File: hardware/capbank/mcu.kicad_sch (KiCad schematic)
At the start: 19 parts, among them J3 Conn_01x02, J4 Conn_01x02, J5 Conn_01x06, SW2 SW_SPST, U6 ATtiny84A-P, Y1 16MHz

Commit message: Small hardware changes
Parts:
- removed TP1: ~, TestPoint:TestPoint_THTPad_1.5x1.5mm_Drill0.7mm, symbol Connector:TestPoint
- removed U6: ATtiny84A-P, Package_DIP:DIP-14_W7.62mm, symbol MCU_Microchip_ATtiny:ATtiny84A-P
- added U8: ATtiny84A-SS, Package_SO:SOIC-14_3.9x8.7mm_P1.27mm, symbol MCU_Microchip_ATtiny:ATtiny84A-SS
- Y1: footprint (none) -> PCM_Crystal_Handsoldering_AKL:Resonator_SMD_muRata_CSTxExxV-3Pin_3.0x1.1mm_BigPads
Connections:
- net GND: now also U8.14 (GND)
- net HVSP_CLK_FSK_IN: now also U8.10 (PA3)
- net HVSP_SDI_RELAY1: now also U8.13 (AREF/PA0)
- net HVSP_SDO_RELAY3: now also U8.11 (PA2)
- net HVSP_SII_RELAY2: now also U8.12 (PA1)
- net PRG_MOSI_I2C_SDA: now also U8.7 (PA6)
- net PRG_SCK_I2C_SCL: now also U8.9 (PA4)
- net SCK: now also U8.5 (PB2)
- net SDI: now also U8.6 (PA7)
- net VDD: now also U8.1 (VCC)
- net XTAL1: now also U8.2 (XTAL1/PB0)
- net XTAL2: now also U8.3 (XTAL2/PB1)
- net ~{CS}: now also U8.8 (PA5)
- net ~{RESET}: now also U8.4 (~{RESET}/PB3)
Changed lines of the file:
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@@
-	)
-	(junction
-		(at 64.77 90.17)
-		(diameter 0)
-		(color 0 0 0 0)
 	)
 	(junction
@@
 	(wire
 		(pts
-			(xy 64.77 90.17) (xy 78.74 90.17)
-		)
-		(stroke
-			(width 0)
-			(type default)
-		)
-	)
-	(wire
-		(pts
 			(xy 195.58 38.1) (xy 195.58 36.83)
 		)
@@
 	(wire
 		(pts
-			(xy 59.69 90.17) (xy 64.77 90.17)
+			(xy 59.69 90.17) (xy 78.74 90.17)
 		)
 		(stroke
@@
 	)
 	(symbol
+		(lib_id "MCU_Microchip_ATtiny:ATtiny84A-SS")
+		(at 243.84 130.81 0)
+		(unit 1)
+		(exclude_from_sim no)
+		(in_bom yes)
+		(on_board yes)
+		(dnp no)
+		(fields_autoplaced yes)
+		(property "Reference" "U8"
+			(at 229.87 129.5399 0)
+			(effects
+				(font
+					(size 1.27 1.27)
+				)
+				(justify right)
+			)
+		)
+		(property "Value" "ATtiny84A-SS"
+			(at 229.87 132.0799 0)
+			(effects
+				(font
+					(size 1.27 1.27)
+				)
+				(justify right)
+			)
+		)
+		(property "Footprint" "Package_SO:SOIC-14_3.9x8.7mm_P1.27mm"
+			(at 243.84 130.81 0)
+			(effects
+				(font
+					(size 1.27 1.27)
+					(italic yes)
+				)
+				(hide yes)
+			)
+		)
+		(property "Datasheet" "http://ww1.microchip.com/downloads/en/DeviceDoc/doc8183.pdf"
+			(at 243.84 130.81 0)
+			(effects
+				(font
+					(size 1.27 1.27)
+				)
+				(hide yes)
+			)
+		)
+		(property "Description" "20MHz, 8kB Flash, 512B SRAM, 512B EEPROM, debugWIRE, SOIC-14"
+			(at 243.84 130.81 0)
+			(effects
+				(font
+					(size 1.27 1.27)
+				)
+				(hide yes)
+			)
+		)
+		(pin "4"
+		)
+		(pin "7"
+		)
+		(pin "2"
+		)
+		(pin "3"
+		)
+		(pin "5"
+		)
+		(pin "8"
+		)
+		(pin "6"
+		)
+		(pin "9"
+		)
+		(pin "10"
+		)
+		(pin "11"
+		)
+		(pin "12"
+		)
+		(pin "13"
+		)
+		(pin "14"
+		)
+		(pin "1"
+		)
+		(instances
+			(project ""
+				(path "/461cb8a1-2d60-44a8-88b5-d61a3ba14a84/d9c36704-5831-4033-b353-abc8255d1c86"
+					(reference "U8")
+					(unit 1)
+				)
+			)
+		)
+	)
+	(symbol
 		(lib_id "power:GND")
 		(at 93.98 97.79 0)
@@
 	)
 	(symbol
-		(lib_id "MCU_Microchip_ATtiny:ATtiny84A-P")
-		(at 243.84 130.81 0)
-		(unit 1)
-		(exclude_from_sim no)
-		(in_bom yes)
-		(on_board yes)
-		(dnp no)
-		(fields_autoplaced yes)
-		(property "Reference" "U6"
-			(at 229.87 129.5399 0)
-			(effects
-				(font
-					(size 1.27 1.27)
-				)
-				(justify right)
-			)
-		)
-		(property "Value" "ATtiny84A-P"
-			(at 229.87 132.0799 0)
-			(effects
-				(font
-					(size 1.27 1.27)
-				)
-				(justify right)
-			)
-		)
-		(property "Footprint" "Package_DIP:DIP-14_W7.62mm"
-			(at 243.84 130.81 0)
-			(effects
-				(font
-					(size 1.27 1.27)
-					(italic yes)
-				)
-				(hide yes)
-			)
-		)
-		(property "Datasheet" "http://ww1.microchip.com/downloads/en/DeviceDoc/doc8183.pdf"
-			(at 243.84 130.81 0)
-			(effects
-				(font
-					(size 1.27 1.27)
-				)
-				(hide yes)
-			)
-		)
-		(property "Description" "20MHz, 8kB Flash, 512B SRAM, 512B EEPROM, debugWIRE, DIP-14"
-			(at 243.84 130.81 0)
-			(effects
-				(font
-					(size 1.27 1.27)
-				)
-				(hide yes)
-			)
-		)
-		(pin "11"
-		)
-		(pin "5"
-		)
-		(pin "12"
-		)
-		(pin "13"
-		)
-		(pin "2"
-		)
-		(pin "8"
-		)
-		(pin "9"
-		)
-		(pin "14"
-		)
-		(pin "6"
-		)
-		(pin "7"
-		)
-		(pin "3"
-		)
-		(pin "4"
-		)
-		(pin "1"
-		)
-		(pin "10"
-		)
-		(instances
-			(project ""
-				(path "/461cb8a1-2d60-44a8-88b5-d61a3ba14a84/d9c36704-5831-4033-b353-abc8255d1c86"
-					(reference "U6")
-					(unit 1)
-				)
-			)
-		)
-	)
-	(symbol
 		(lib_id "power:GND")
 		(at 58.42 57.15 0)
@@
 			)
 		)
-		(property "Footprint" ""
+		(property "Footprint" "PCM_Crystal_Handsoldering_AKL:Resonator_SMD_muRata_CSTxExxV-3Pin_3.0x1.1mm_BigPads"
 			(at 179.705 135.89 0)
 			(effects
@@
 					(unit 1)
 				)
-			)
-		)
-	)
-	(symbol
-		(lib_id "Connector:TestPoint")
-		(at 64.77 90.17 0)
-		(unit 1)
-		(exclude_from_sim no)
-		(in_bom yes)
-		(on_board yes)
-		(dnp no)
-		(fields_autoplaced yes)
-		(property "Reference" "TP1"
-			(at 67.31 85.5979 0)
-			(effects
-				(font
-					(size 1.27 1.27)
-				)
-				(justify left)
-			)
-		)
-		(property "Value" "~"
-			(at 67.31 88.1379 0)
-			(effects
-				(font
-					(size 1.27 1.27)
-				)
-				(justify left)
-			)
-		)
-		(property "Footprint" "TestPoint:TestPoint_THTPad_1.5x1.5mm_Drill0.7mm"
-			(at 69.85 90.17 0)
-			(effects
-				(font
-					(size 1.27 1.27)
-				)
-				(hide yes)
-			)
-		)
-		(property "Datasheet" "~"
-			(at 69.85 90.17 0)
-			(effects
-				(font
-					(size 1.27 1.27)
-				)
-				(hide yes)
-			)
-		)
-		(property "Description" "test point"
-			(at 64.77 90.17 0)
-			(effects
-				(font
-					(size 1.27 1.27)
-				)
-				(hide yes)
-			)
-		)
-		(pin "1"
-		)
-		(instances
-			(project "capbank1"
-				(path "/461cb8a1-2d60-44a8-88b5-d61a3ba14a84/d9c36704-5831-4033-b353-abc8255d1c86"
-					(reference "TP1")
-					(unit 1)
-				)

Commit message: Add footprint for buffered-filter and replace pot with digital pot
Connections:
- net PRG_MOSI_I2C_SDA renamed PRG_MOSI_RHEO_UD
- net PRG_SCK_I2C_SCL renamed PRG_SCK_RHEO_CS
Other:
- sheet FSK Demod ports: added RHEO_CS, RHEO_UD; removed none
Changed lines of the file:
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@@
+	(wire
+		(pts
+			(xy 58.42 151.13) (xy 64.77 151.13)
+		)
+		(stroke
+			(width 0)
+			(type default)
+		)
+	)
 	(wire
 		(pts
@@
 		(pts
 			(xy 259.08 140.97) (xy 262.89 140.97)
+		)
+		(stroke
+			(width 0)
+			(type default)
+		)
+	)
+	(wire
+		(pts
+			(xy 58.42 148.59) (xy 64.77 148.59)
 		)
 		(stroke
@@
 		)
 	)
-	(label "PRG_MOSI_I2C_SDA"
+	(label "PRG_MOSI_RHEO_UD"
 		(at 58.42 52.07 0)
 		(effects
@@
 		)
 	)
+	(label "PRG_SCK_RHEO_CS"
+		(at 58.42 148.59 180)
+		(effects
+			(font
+				(size 1.27 1.27)
+			)
+			(justify right bottom)
+		)
+	)
 	(label "FSK"
 		(at 58.42 143.51 180)
@@
 		)
 	)
-	(label "PRG_MOSI_I2C_SDA"
+	(label "PRG_MOSI_RHEO_UD"
 		(at 262.89 130.81 0)
 		(effects
@@
 		)
 	)
+	(label "PRG_MOSI_RHEO_UD"
+		(at 58.42 151.13 180)
+		(effects
+			(font
+				(size 1.27 1.27)
+			)
+			(justify right bottom)
+		)
+	)
 	(label "HVSP_SDI_RELAY1"
 		(at 251.46 29.21 180)
@@
 		)
 	)
-	(label "PRG_SCK_I2C_SCL"
+	(label "PRG_SCK_RHEO_CS"
 		(at 262.89 125.73 0)
 		(effects
@@
 		)
 	)
-	(label "PRG_SCK_I2C_SCL"
+	(label "PRG_SCK_RHEO_CS"
 		(at 58.42 46.99 0)
 		(effects
@@
 	(sheet
 		(at 64.77 139.7)
-		(size 27.94 7.62)
+		(size 27.94 22.86)
 		(exclude_from_sim no)
 		(in_bom yes)
@@
 		)
 		(property "Sheetfile" "fsk_demod.kicad_sch"
-			(at 64.77 147.9046 0)
+			(at 64.77 163.1446 0)
 			(effects
 				(font
@@
 			)
 		)
+		(pin "RHEO_CS" input
+			(at 64.77 148.59 180)
+			(effects
+				(font
+					(size 1.27 1.27)
+				)
+				(justify left)
+			)
+		)
+		(pin "RHEO_UD" input
+			(at 64.77 151.13 180)
+			(effects
+				(font
+					(size 1.27 1.27)
+				)
+				(justify left)
+			)
+		)

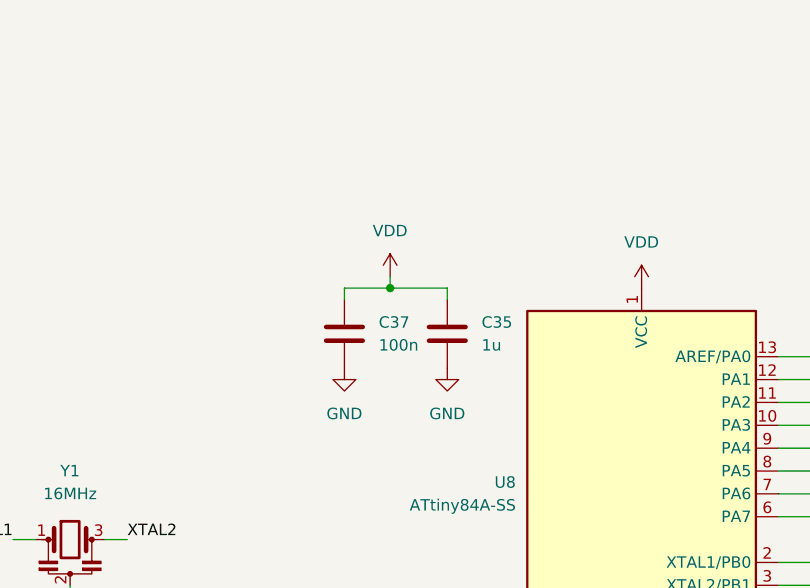
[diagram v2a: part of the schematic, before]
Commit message: Add hysteresis to comparator
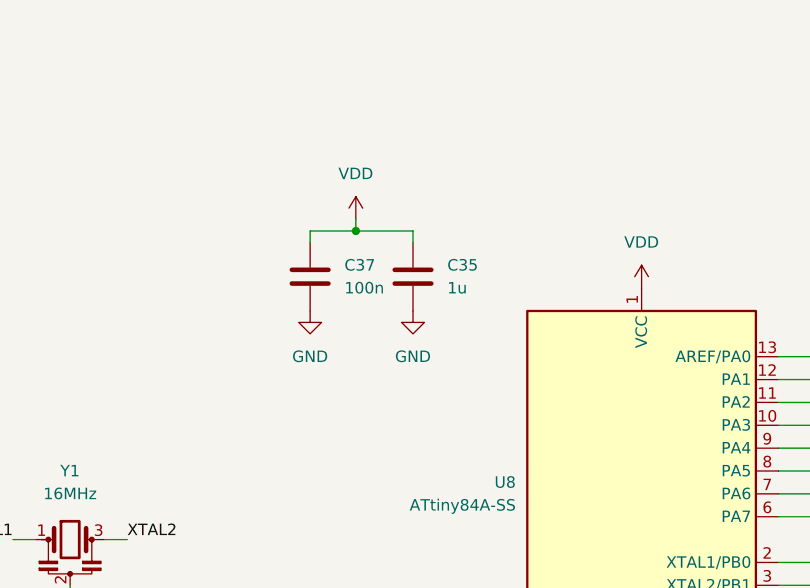
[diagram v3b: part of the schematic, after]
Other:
- moved on the sheet: C35, C37
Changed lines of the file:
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@@
 	)
 	(junction
-		(at 215.9 107.95)
+		(at 212.09 101.6)
 		(diameter 0)
 		(color 0 0 0 0)
@@
 	(wire
 		(pts
-			(xy 215.9 107.95) (xy 222.25 107.95)
+			(xy 212.09 101.6) (xy 218.44 101.6)
 		)
 		(stroke
@@
 	(wire
 		(pts
-			(xy 210.82 107.95) (xy 215.9 107.95)
+			(xy 207.01 101.6) (xy 212.09 101.6)
 		)
 		(stroke
@@
 	(wire
 		(pts
-			(xy 210.82 109.22) (xy 210.82 107.95)
+			(xy 207.01 102.87) (xy 207.01 101.6)
 		)
 		(stroke
@@
 	(wire
 		(pts
-			(xy 215.9 106.68) (xy 215.9 107.95)
+			(xy 212.09 100.33) (xy 212.09 101.6)
 		)
 		(stroke
@@
 	(wire
 		(pts
-			(xy 222.25 109.22) (xy 222.25 107.95)
+			(xy 218.44 102.87) (xy 218.44 101.6)
 		)
 		(stroke
@@
 	(symbol
 		(lib_id "Device:C")
-		(at 210.82 113.03 0)
+		(at 207.01 106.68 0)
 		(unit 1)
 		(exclude_from_sim no)
@@
 		(fields_autoplaced yes)
 		(property "Reference" "C37"
-			(at 214.63 111.7599 0)
+			(at 210.82 105.4099 0)
 			(effects
 				(font
@@
 		)
 		(property "Value" "100n"
-			(at 214.63 114.2999 0)
+			(at 210.82 107.9499 0)
 			(effects
 				(font
@@
 		)
 		(property "Footprint" "PCM_Capacitor_SMD_AKL:C_0603_1608Metric"
-			(at 211.7852 116.84 0)
+			(at 207.9752 110.49 0)
 			(effects
 				(font
@@
 		)
 		(property "Datasheet" "~"
-			(at 210.82 113.03 0)
+			(at 207.01 106.68 0)
 			(effects
 				(font
@@
 		)
 		(property "Description" "Unpolarized capacitor"
-			(at 210.82 113.03 0)
+			(at 207.01 106.68 0)
 			(effects
 				(font
@@
 	(symbol
 		(lib_id "Device:C")
-		(at 222.25 113.03 0)
+		(at 218.44 106.68 0)
 		(unit 1)
 		(exclude_from_sim no)
@@
 		(fields_autoplaced yes)
 		(property "Reference" "C35"
-			(at 226.06 111.7599 0)
+			(at 222.25 105.4099 0)
 			(effects
 				(font
@@
 		)
 		(property "Value" "1u"
-			(at 226.06 114.2999 0)
+			(at 222.25 107.9499 0)
 			(effects
 				(font
@@
 		)
 		(property "Footprint" "PCM_Capacitor_SMD_AKL:C_0603_1608Metric"
-			(at 223.2152 116.84 0)
+			(at 219.4052 110.49 0)
 			(effects
 				(font
@@
 		)
 		(property "Datasheet" "~"
-			(at 222.25 113.03 0)
+			(at 218.44 106.68 0)
 			(effects
 				(font
@@
 		)
 		(property "Description" "Unpolarized capacitor"
-			(at 222.25 113.03 0)
+			(at 218.44 106.68 0)
 			(effects
 				(font
@@
 	(symbol
 		(lib_id "power:GND")
-		(at 222.25 116.84 0)
+		(at 218.44 110.49 0)
 		(unit 1)
 		(exclude_from_sim no)
@@
 		(fields_autoplaced yes)
 		(property "Reference" "#PWR095"
-			(at 222.25 123.19 0)
+			(at 218.44 116.84 0)
 			(effects
 				(font
@@
 		)
 		(property "Value" "GND"
-			(at 222.25 121.92 0)
+			(at 218.44 115.57 0)
 			(effects
 				(font
@@
 		)
 		(property "Footprint" ""
-			(at 222.25 116.84 0)
+			(at 218.44 110.49 0)
 			(effects
 				(font
@@
 		)
 		(property "Datasheet" ""
-			(at 222.25 116.84 0)
+			(at 218.44 110.49 0)
 			(effects
 				(font
@@
 		)
 		(property "Description" "Power symbol creates a global label with name \"GND\" , ground"
-			(at 222.25 116.84 0)
+			(at 218.44 110.49 0)
 			(effects
 				(font
@@
 	(symbol
 		(lib_id "power:VDD")
-		(at 215.9 106.68 0)
+		(at 212.09 100.33 0)
 		(unit 1)
 		(exclude_from_sim no)
@@
 		(dnp no)
 		(property "Reference" "#PWR011"
-			(at 215.9 110.49 0)
+			(at 212.09 104.14 0)
 			(effects
 				(font
@@
 		)
 		(property "Value" "VDD"
-			(at 215.9 101.6 0)
+			(at 212.09 95.25 0)
 			(effects
 				(font
@@
 		)
 		(property "Footprint" ""
-			(at 215.9 106.68 0)
+			(at 212.09 100.33 0)
 			(effects
 				(font
@@
 		)
 		(property "Datasheet" ""
-			(at 215.9 106.68 0)
+			(at 212.09 100.33 0)
 			(effects
 				(font
@@
 		)
 		(property "Description" "Power symbol creates a global label with name \"VDD\""
-			(at 215.9 106.68 0)
+			(at 212.09 100.33 0)
 			(effects
 				(font
@@
 	(symbol
 		(lib_id "power:GND")
-		(at 210.82 116.84 0)
+		(at 207.01 110.49 0)
 		(unit 1)
 		(exclude_from_sim no)
@@
 		(fields_autoplaced yes)
 		(property "Reference" "#PWR0106"
-			(at 210.82 123.19 0)
+			(at 207.01 116.84 0)
 			(effects
 				(font
@@
 		)
 		(property "Value" "GND"
-			(at 210.82 121.92 0)
+			(at 207.01 115.57 0)
 			(effects
 				(font
@@
 		)
 		(property "Footprint" ""
-			(at 210.82 116.84 0)
+			(at 207.01 110.49 0)
 			(effects
 				(font
@@
 		)
 		(property "Datasheet" ""
-			(at 210.82 116.84 0)
+			(at 207.01 110.49 0)
 			(effects
 				(font
@@
 		)
 		(property "Description" "Power symbol creates a global label with name \"GND\" , ground"
-			(at 210.82 116.84 0)
-			(effects
-				(font
+			(at 207.01 110.49 0)
+			(effects
+				(font

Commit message: Various wiring fixes and add bleed resistor to antenna
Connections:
- net HVSP_SDI_RELAY1 is gone; now on net RELAY1: JP5.1 (A), U8.13 (AREF/PA0)
- net HVSP_SDO_RELAY3 is gone; now on net RELAY3: JP7.1 (A), U8.11 (PA2)
- net HVSP_SII_RELAY2 is gone; now on net RELAY2: JP6.1 (A), U8.12 (PA1)
- net PRG_MOSI_RHEO_UD is gone; now on net SDI: J5.3 (Pin_3), U8.7 (PA6)
- net PRG_SCK_RHEO_CS is gone; now on net SCK: J5.5 (Pin_5), U8.9 (PA4)
- net RELAY1: no longer JP5.2 (B)
- net RELAY2: no longer JP6.2 (B)
- net RELAY3: no longer JP7.2 (B)
- net SCK: no longer U8.5 (PB2)
- net SDI: no longer U8.6 (PA7)
- net HVSP_CLK_FSK_IN renamed FSK_IN
- new net ORELAY1: JP5.2 (B)
- new net ORELAY2: JP6.2 (B)
- new net ORELAY3: JP7.2 (B)
- new net RHEO_CS: U8.5 (PB2)
- new net RHEO_UD: U8.6 (PA7)
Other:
- moved on the sheet: C35, C37, U8, Y1
